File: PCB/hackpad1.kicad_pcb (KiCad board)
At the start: 2 copper layers, 82.5 x 106 mm, 33 parts, among them SW1 SW_Push, SW10 SW_Push, SW11 SW_Push, SW12 SW_Push, SW13 SW_Push, SW14 SW_Push, SW15 SW_Push, SW16 SW_Push, SW2 SW_Push, SW3 SW_Push, SW4 SW_Push, SW5 SW_Push, SW6 SW_Push, SW7 SW_Push, SW8 SW_Push, SW9 SW_Push, U1 MOUDLE-SEEEDUINO-XIAO

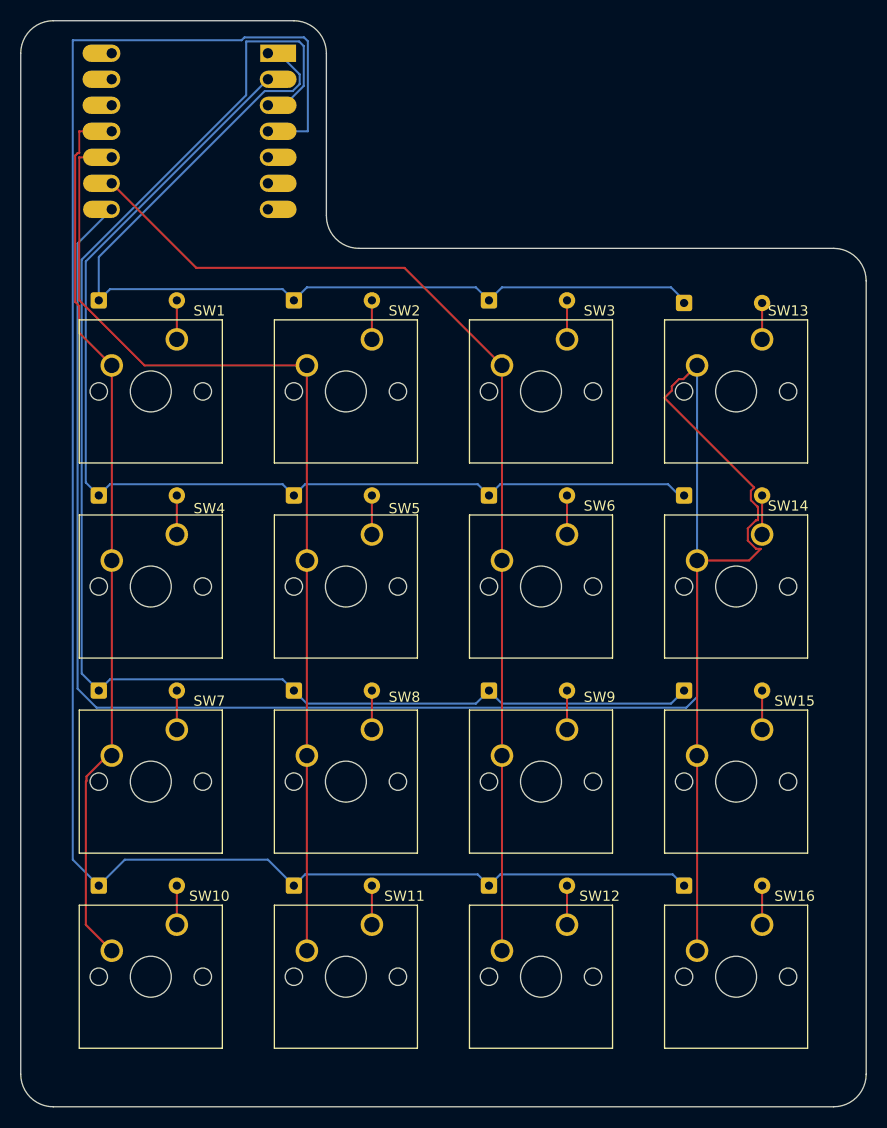
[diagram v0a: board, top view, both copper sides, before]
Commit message: updated PCB design to fit requirements for stardance
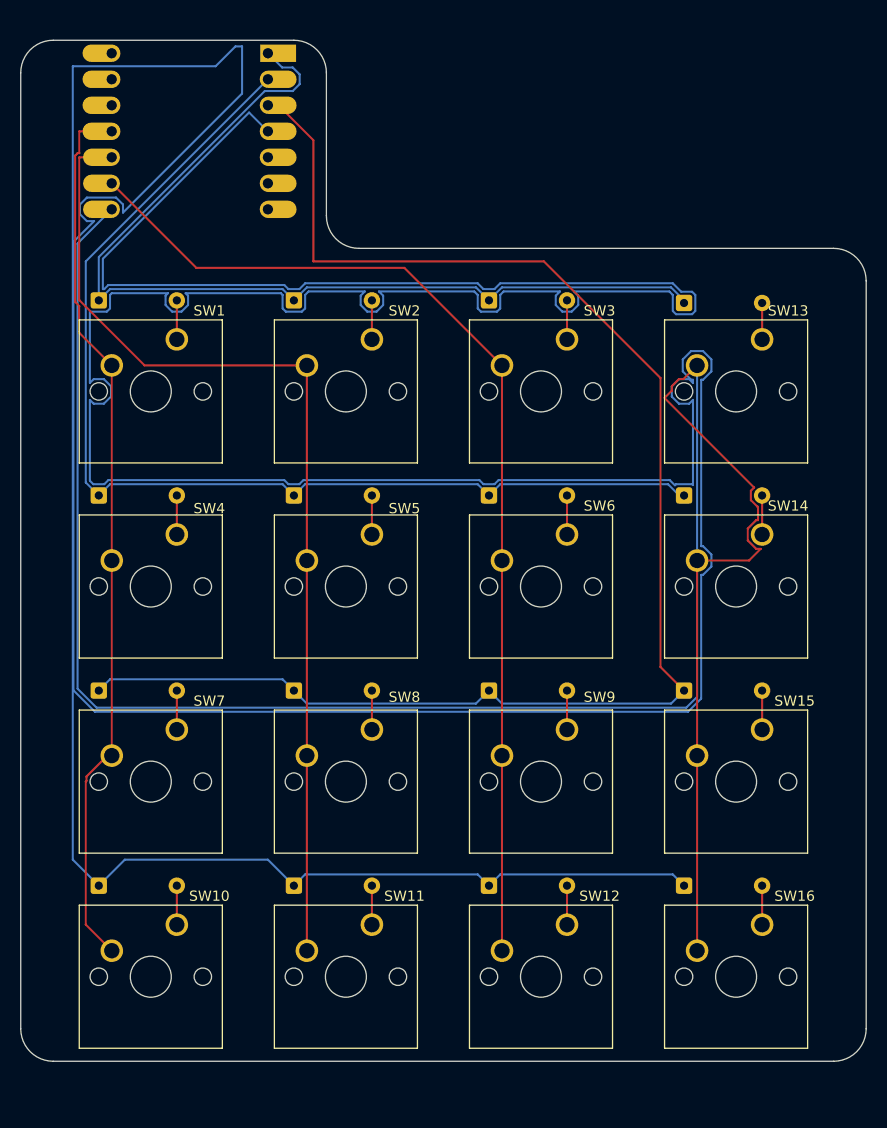
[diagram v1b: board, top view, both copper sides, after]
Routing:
- net Net-(D16-K): track 180.6 -> 602.3 mm
- net Net-(D1-K): track 144.9 -> 147.9 mm
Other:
- board size 82.5 x 106 mm -> 82.5 x 99.7 mm
